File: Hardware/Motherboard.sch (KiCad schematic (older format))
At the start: 22 parts, among them J2 Conn_01x05_Male, J5 Conn_01x04_Male, SW1 SW_Push, SW2 SW_Push, SW3 SW_Push, U1 PIC18F46K22-xPT

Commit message: [Hardware] Added all schematic parts (but not all external parts, like display or female connectors).
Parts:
- added C15: 100n, Capacitor_SMD:C_1206_3216Metric_Pad1.42x1.75mm_HandSolder, symbol Device:C
- added J6: Conn_01x02_Male, Connector_PinHeader_2.54mm:PinHeader_1x02_P2.54mm_Vertical, symbol Connector:Conn_01x02_Male
- J5: footprint (none) -> Connector_PinHeader_2.54mm:PinHeader_1x04_P2.54mm_Vertical
- SW1, SW2, SW3: footprint (none) -> Button_Switch_THT:SW_Tactile_SKHH_Angled
- gave numbers to parts that had none: 3
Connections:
- net +5V: now also C15.1, J6.1 (Pin_1)
- net GND: now also C15.2, J6.2 (Pin_2)
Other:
- note added: "USB power connector.\nUSB D+ and D- are not connected."
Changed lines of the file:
@@
 F 0 "J5" H 5700 6650 50  0000 R CNN
 F 1 "Conn_01x04_Male" H 5700 6750 50  0000 R CNN
-F 2 "" H 5600 6450 50  0001 C CNN
+F 2 "Connector_PinHeader_2.54mm:PinHeader_1x04_P2.54mm_Vertical" H 5600 6450 50  0001 C CNN
 F 3 "~" H 5600 6450 50  0001 C CNN
 	1    5600 6450
@@
 F 0 "SW2" V 2404 1848 50  0000 L CNN
 F 1 "SW_Push" V 2495 1848 50  0000 L CNN
-F 2 "" H 2450 1900 50  0001 C CNN
+F 2 "Button_Switch_THT:SW_Tactile_SKHH_Angled" H 2450 1900 50  0001 C CNN
 F 3 "~" H 2450 1900 50  0001 C CNN
 	1    2450 1700
@@
 F 0 "SW1" V 1804 1848 50  0000 L CNN
 F 1 "SW_Push" V 1895 1848 50  0000 L CNN
-F 2 "" H 1850 1900 50  0001 C CNN
+F 2 "Button_Switch_THT:SW_Tactile_SKHH_Angled" H 1850 1900 50  0001 C CNN
 F 3 "~" H 1850 1900 50  0001 C CNN
 	1    1850 1700
@@
 F 0 "SW3" V 2154 6448 50  0000 L CNN
 F 1 "SW_Push" V 2245 6448 50  0000 L CNN
-F 2 "" H 2200 6500 50  0001 C CNN
+F 2 "Button_Switch_THT:SW_Tactile_SKHH_Angled" H 2200 6500 50  0001 C CNN
 F 3 "~" H 2200 6500 50  0001 C CNN
 	1    2200 6300
@@
 SETTINGS_BUTTON
 $Comp
-L Device:C C?
+L Device:C C12
 U 1 1 5E7D4835
 P 1650 6300
-F 0 "C?" H 1535 6163 50  0000 R CNN
+F 0 "C12" H 1535 6163 50  0000 R CNN
 F 1 "100n" H 1535 6254 50  0000 R CNN
 F 2 "Capacitor_SMD:C_1206_3216Metric_Pad1.42x1.75mm_HandSolder" H 1688 6150 50  0001 C CNN
@@
 $EndComp
 $Comp
-L Device:C C?
+L Device:C C14
 U 1 1 5E7FE585
 P 4950 6700
-F 0 "C?" H 4835 6563 50  0000 R CNN
+F 0 "C14" H 4835 6563 50  0000 R CNN
 F 1 "100n" H 4835 6654 50  0000 R CNN
 F 2 "Capacitor_SMD:C_1206_3216Metric_Pad1.42x1.75mm_HandSolder" H 4988 6550 50  0001 C CNN
@@
 $EndComp
 $Comp
-L Device:C C?
+L Device:C C13
 U 1 1 5E7FF03B
 P 4450 6700
-F 0 "C?" H 4335 6563 50  0000 R CNN
+F 0 "C13" H 4335 6563 50  0000 R CNN
 F 1 "100n" H 4335 6654 50  0000 R CNN
 F 2 "Capacitor_SMD:C_1206_3216Metric_Pad1.42x1.75mm_HandSolder" H 4488 6550 50  0001 C CNN
@@
 	4950 5800 4950 5850
 Connection ~ 4700 5800
+$Comp
+L Connector:Conn_01x02_Male J6
+U 1 1 5E84D5D2
+P 8800 1000
+F 0 "J6" H 8772 974 50  0000 R CNN
+F 1 "Conn_01x02_Male" H 8772 883 50  0000 R CNN
+F 2 "Connector_PinHeader_2.54mm:PinHeader_1x02_P2.54mm_Vertical" H 8800 1000 50  0001 C CNN
+F 3 "~" H 8800 1000 50  0001 C CNN
+	1    8800 1000
+	-1   0    0    -1
+$EndComp
+Text Notes 9600 1100 0    50   ~ 0
+USB power connector.\nUSB D+ and D- are not connected.
+$Comp
+L Device:C C15
+U 1 1 5E853C46
+P 8100 1050
+F 0 "C15" H 8215 1187 50  0000 L CNN
+F 1 "100n" H 8215 1096 50  0000 L CNN
+F 2 "Capacitor_SMD:C_1206_3216Metric_Pad1.42x1.75mm_HandSolder" H 8138 900 50  0001 C CNN
+F 3 "~" H 8100 1050 50  0001 C CNN
+F 4 "25V" H 8215 1005 50  0000 L CNN "Champ4"
+F 5 "X7R" H 8215 914 50  0000 L CNN "Champ5"
+	1    8100 1050
+	1    0    0    -1
+$EndComp
+$Comp
+L power:+5V #PWR09
+U 1 1 5E8541BC
+P 8100 800
+F 0 "#PWR09" H 8100 650 50  0001 C CNN
+F 1 "+5V" H 8115 973 50  0000 C CNN
+F 2 "" H 8100 800 50  0001 C CNN
+F 3 "" H 8100 800 50  0001 C CNN
+	1    8100 800
+	1    0    0    -1
+$EndComp
+$Comp
+L power:GND #PWR010
+U 1 1 5E854558
+P 8100 1300
+F 0 "#PWR010" H 8100 1050 50  0001 C CNN
+F 1 "GND" H 8105 1127 50  0000 C CNN
+F 2 "" H 8100 1300 50  0001 C CNN
+F 3 "" H 8100 1300 50  0001 C CNN
+	1    8100 1300
+	1    0    0    -1
+$EndComp
+Wire Wire Line
+	8100 800  8100 850
+Wire Wire Line
+	8100 850  8550 850
+Wire Wire Line
+	8550 850  8550 1000
+Wire Wire Line
+	8550 1000 8600 1000
+Connection ~ 8100 850
+Wire Wire Line
+	8100 850  8100 900
+Wire Wire Line
+	8600 1100 8550 1100
+Wire Wire Line
+	8550 1100 8550 1250
+Wire Wire Line
+	8550 1250 8100 1250
+Wire Wire Line
+	8100 1250 8100 1200
+Wire Wire Line
+	8100 1250 8100 1300
+Connection ~ 8100 1250
 $EndSCHEMATC

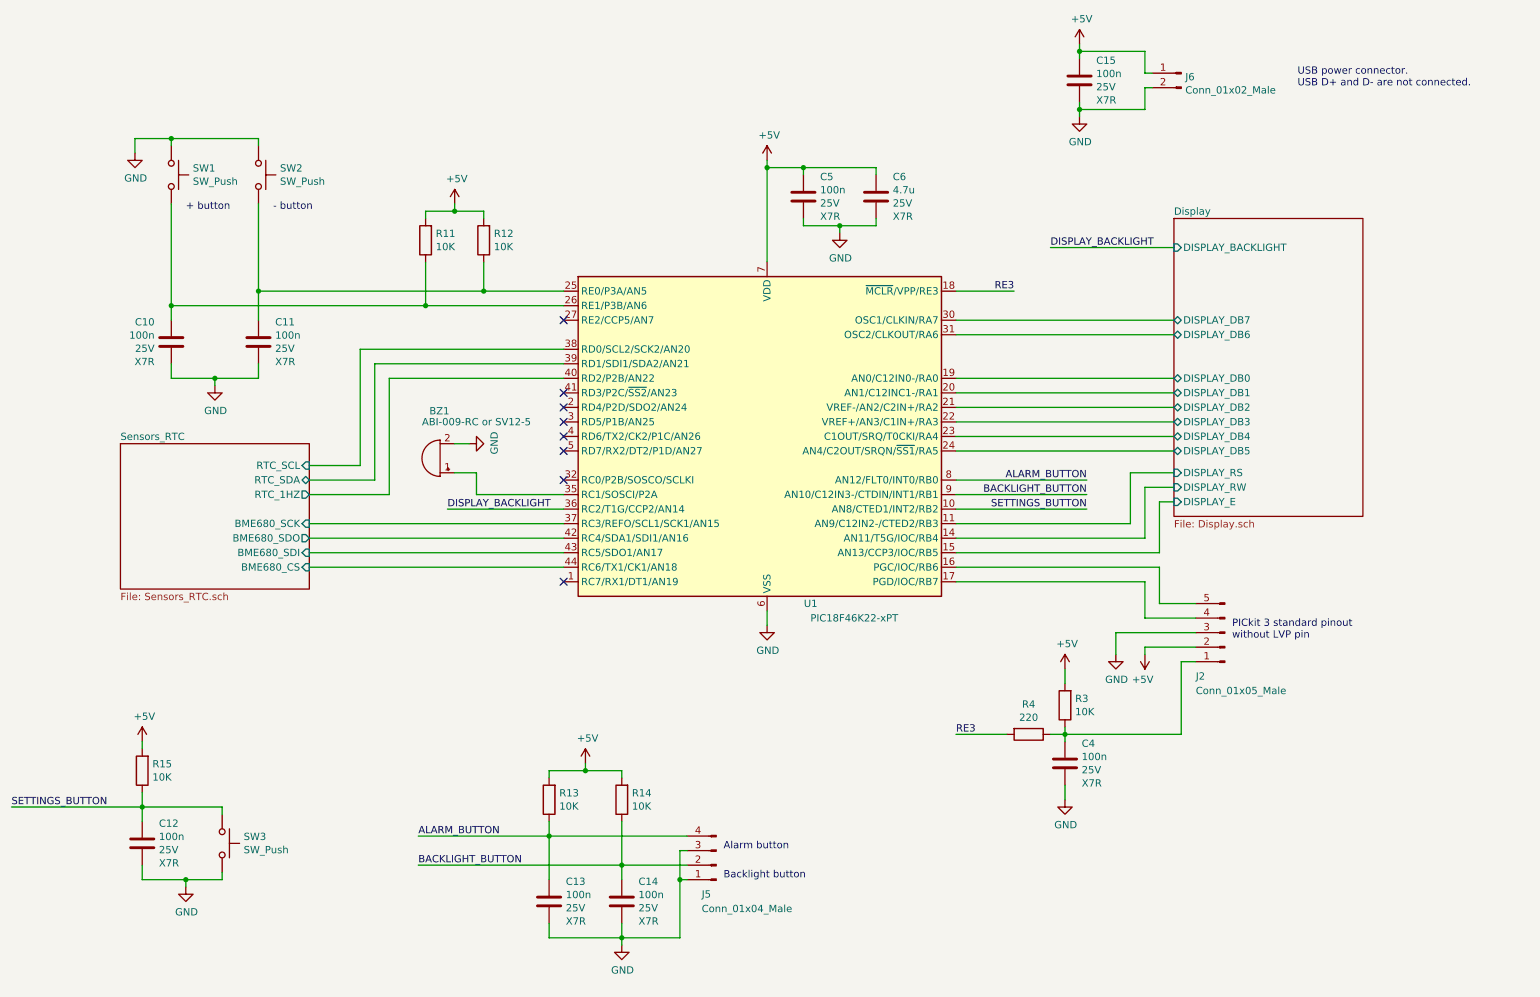
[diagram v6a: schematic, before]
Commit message: [Hardware] Started PCB routing. Components are placed, BME680 board mounting holes are in position, some nets are connected.
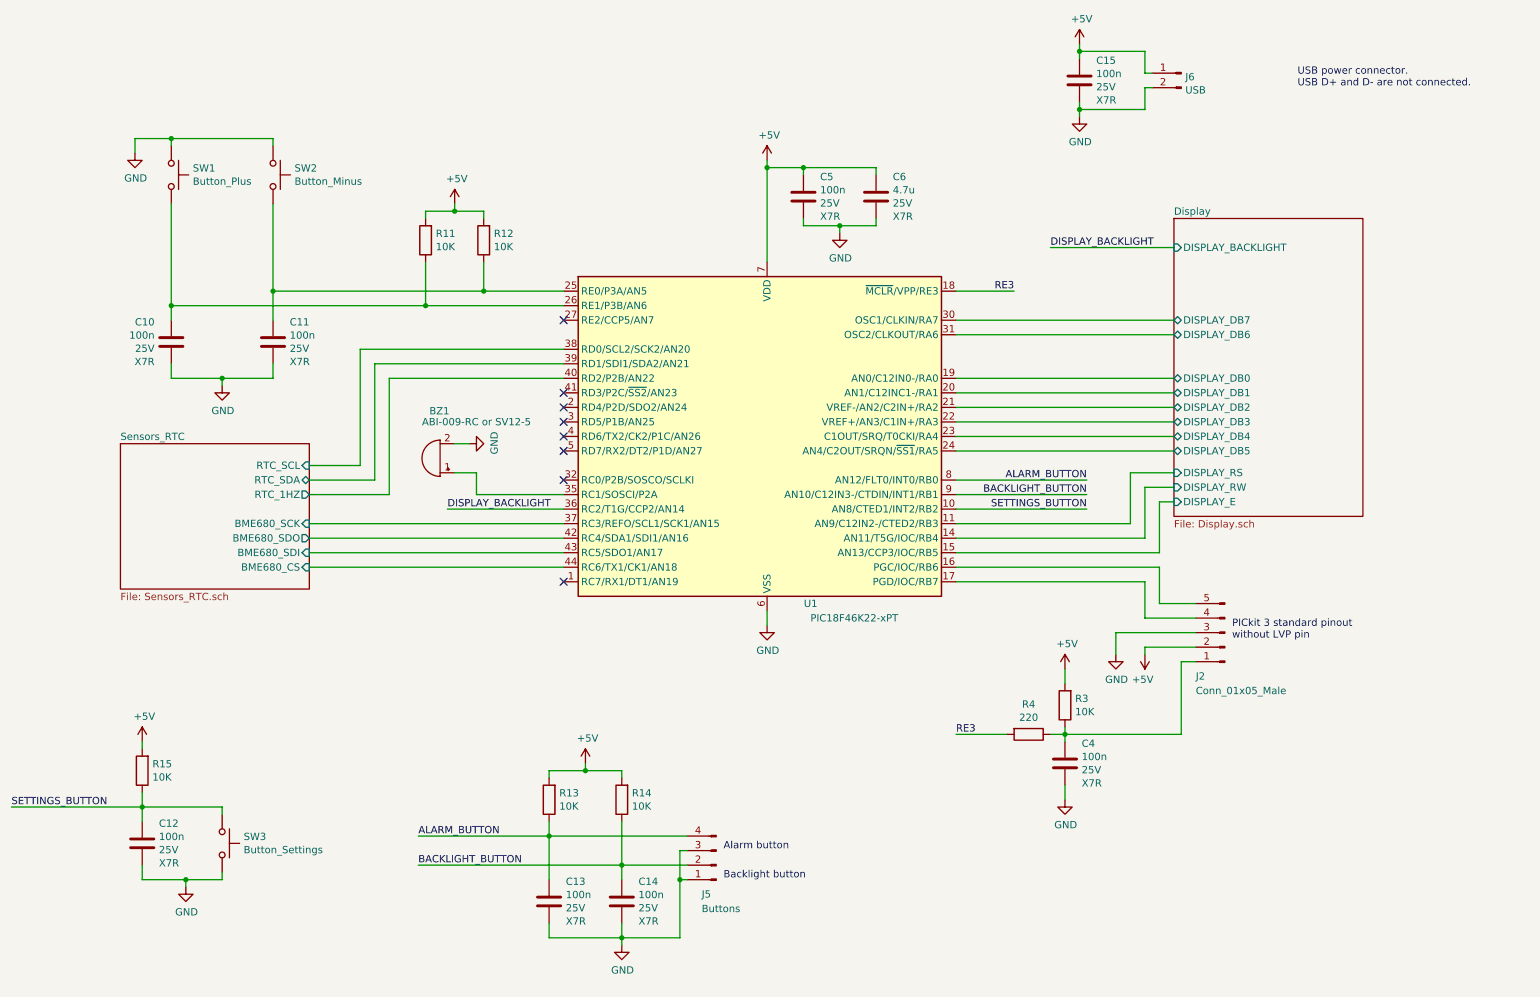
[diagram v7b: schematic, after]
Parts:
- J5: value Conn_01x04_Male -> Buttons
- J6: value Conn_01x02_Male -> USB
- SW1: value SW_Push -> Button_Plus
- SW2: value SW_Push -> Button_Minus
- SW3: value SW_Push -> Button_Settings
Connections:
- net GND: now also SW3.1; no longer SW3.2
- net SETTINGS_BUTTON: now also SW3.2; no longer SW3.1
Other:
- note removed: "+ button"
- note removed: "- button"
- moved on the sheet: C11, SW2
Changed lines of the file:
@@
 P 5600 6450
 F 0 "J5" H 5700 6650 50  0000 R CNN
-F 1 "Conn_01x04_Male" H 5700 6750 50  0000 R CNN
+F 1 "Buttons" H 5700 6750 50  0000 R CNN
 F 2 "Connector_PinHeader_2.54mm:PinHeader_1x04_P2.54mm_Vertical" H 5600 6450 50  0001 C CNN
 F 3 "~" H 5600 6450 50  0001 C CNN
@@
 L Switch:SW_Push SW2
 U 1 1 5E86087F
-P 2450 1700
-F 0 "SW2" V 2404 1848 50  0000 L CNN
-F 1 "SW_Push" V 2495 1848 50  0000 L CNN
-F 2 "Button_Switch_THT:SW_Tactile_SKHH_Angled" H 2450 1900 50  0001 C CNN
-F 3 "~" H 2450 1900 50  0001 C CNN
-	1    2450 1700
+P 2550 1700
+F 0 "SW2" V 2504 1848 50  0000 L CNN
+F 1 "Button_Minus" V 2595 1848 50  0000 L CNN
+F 2 "Button_Switch_THT:SW_Tactile_SKHH_Angled" H 2550 1900 50  0001 C CNN
+F 3 "~" H 2550 1900 50  0001 C CNN
+	1    2550 1700
 	0    1    1    0
 $EndComp
@@
 P 1850 1700
 F 0 "SW1" V 1804 1848 50  0000 L CNN
-F 1 "SW_Push" V 1895 1848 50  0000 L CNN
+F 1 "Button_Plus" V 1895 1848 50  0000 L CNN
 F 2 "Button_Switch_THT:SW_Tactile_SKHH_Angled" H 1850 1900 50  0001 C CNN
 F 3 "~" H 1850 1900 50  0001 C CNN
@@
 U 1 1 5E864A28
 P 2200 6300
-F 0 "SW3" V 2154 6448 50  0000 L CNN
-F 1 "SW_Push" V 2245 6448 50  0000 L CNN
+F 0 "SW3" V 2246 6448 50  0000 L CNN
+F 1 "Button_Settings" V 2155 6448 50  0000 L CNN
 F 2 "Button_Switch_THT:SW_Tactile_SKHH_Angled" H 2200 6500 50  0001 C CNN
 F 3 "~" H 2200 6500 50  0001 C CNN
 	1    2200 6300
-	0    1    1    0
-$EndComp
-Wire Wire Line
-	2450 2500 4000 2500
+	0    1    -1   0
+$EndComp
+Wire Wire Line
+	2550 2500 4000 2500
 Wire Wire Line
 	4550 2600 3600 2600
 Wire Wire Line
-	2450 1500 2450 1450
-Wire Wire Line
-	2450 1450 1850 1450
+	2550 1500 2550 1450
+Wire Wire Line
+	2550 1450 1850 1450
 Wire Wire Line
 	1850 1450 1850 1500
@@
 L Device:C C11
 U 1 1 5E8AB83D
-P 2450 2850
-F 0 "C11" H 2335 2713 50  0000 R CNN
-F 1 "100n" H 2335 2804 50  0000 R CNN
-F 2 "Capacitor_SMD:C_1206_3216Metric_Pad1.42x1.75mm_HandSolder" H 2488 2700 50  0001 C CNN
-F 3 "~" H 2450 2850 50  0001 C CNN
-F 4 "25V" H 2335 2895 50  0000 R CNN "Champ4"
-F 5 "X7R" H 2335 2986 50  0000 R CNN "Champ5"
-	1    2450 2850
+P 2550 2850
+F 0 "C11" H 2435 2713 50  0000 R CNN
+F 1 "100n" H 2435 2804 50  0000 R CNN
+F 2 "Capacitor_SMD:C_1206_3216Metric_Pad1.42x1.75mm_HandSolder" H 2588 2700 50  0001 C CNN
+F 3 "~" H 2550 2850 50  0001 C CNN
+F 4 "25V" H 2435 2895 50  0000 R CNN "Champ4"
+F 5 "X7R" H 2435 2986 50  0000 R CNN "Champ5"
+	1    2550 2850
 	-1   0    0    1
 $EndComp
@@
 L power:GND #PWR03
 U 1 1 5E8AE348
-P 2150 3150
-F 0 "#PWR03" H 2150 2900 50  0001 C CNN
-F 1 "GND" H 2155 2977 50  0000 C CNN
-F 2 "" H 2150 3150 50  0001 C CNN
-F 3 "" H 2150 3150 50  0001 C CNN
-	1    2150 3150
+P 2200 3150
+F 0 "#PWR03" H 2200 2900 50  0001 C CNN
+F 1 "GND" H 2205 2977 50  0000 C CNN
+F 2 "" H 2200 3150 50  0001 C CNN
+F 3 "" H 2200 3150 50  0001 C CNN
+	1    2200 3150
 	1    0    0    -1
 $EndComp
@@
 	1850 3000 1850 3100
 Wire Wire Line
-	2450 3100 2450 3000
+	2550 3100 2550 3000
 $Comp
 L power:GND #PWR01
@@
 	1600 1550 1600 1450
 Wire Wire Line
-	2450 1900 2450 2500
-Wire Wire Line
-	2450 2500 2450 2700
-Connection ~ 2450 2500
+	2550 1900 2550 2500
+Wire Wire Line
+	2550 2500 2550 2700
+Connection ~ 2550 2500
 Wire Wire Line
 	1850 2700 1850 2600
@@
 NoConn ~ 4550 3200
 Wire Wire Line
-	1850 3100 2150 3100
+	1850 3100 2200 3100
 Wire Wire Line
 	1600 1450 1850 1450
 Connection ~ 1850 1450
 Wire Wire Line
-	2150 3150 2150 3100
-Connection ~ 2150 3100
-Wire Wire Line
-	2150 3100 2450 3100
-Text Notes 1950 1950 0    50   ~ 0
-+ button
-Text Notes 2550 1950 0    50   ~ 0
-- button
+	2200 3150 2200 3100
+Connection ~ 2200 3100
+Wire Wire Line
+	2200 3100 2550 3100
 $Comp
 L Device:R R?
@@
 P 8800 1000
 F 0 "J6" H 8772 974 50  0000 R CNN
-F 1 "Conn_01x02_Male" H 8772 883 50  0000 R CNN
+F 1 "USB" H 8772 883 50  0000 R CNN
 F 2 "Connector_PinHeader_2.54mm:PinHeader_1x02_P2.54mm_Vertical" H 8800 1000 50  0001 C CNN
 F 3 "~" H 8800 1000 50  0001 C CNN

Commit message: [Hardware] Moved buttons to another schematic sheet and fully routed PCB.
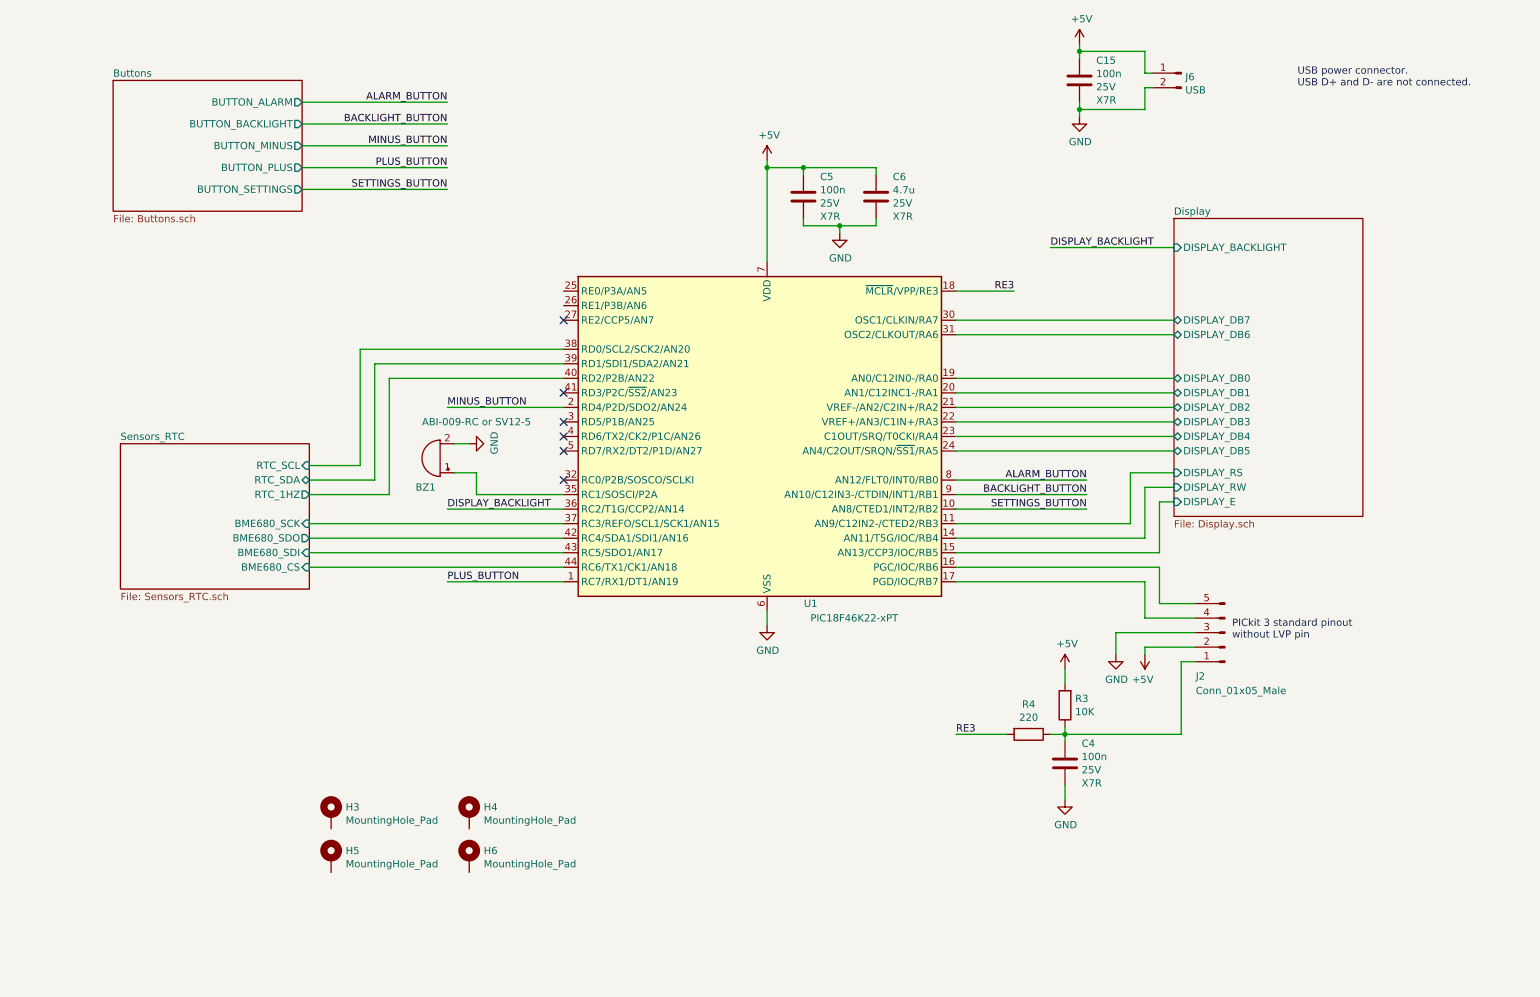
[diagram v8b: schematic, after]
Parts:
- removed C10, C11, C12, C13, C14: 100n, Capacitor_SMD:C_1206_3216Metric_Pad1.42x1.75mm_HandSolder, symbol Device:C
- removed J5: Buttons, Connector_PinHeader_2.54mm:PinHeader_1x04_P2.54mm_Vertical, symbol Connector:Conn_01x04_Male
- removed R11, R12, R13, R14, R15: 10K, Resistor_SMD:R_1206_3216Metric_Pad1.42x1.75mm_HandSolder, symbol Device:R
- removed SW1: Button_Plus, Button_Switch_THT:SW_Tactile_SKHH_Angled, symbol Switch:SW_Push
- removed SW2: Button_Minus, Button_Switch_THT:SW_Tactile_SKHH_Angled, symbol Switch:SW_Push
- removed SW3: Button_Settings, Button_Switch_THT:SW_Tactile_SKHH_Angled, symbol Switch:SW_Push
- added H3, H4, H5, H6: MountingHole_Pad, MountingHole:MountingHole_4.5mm_Pad, symbol Mechanical:MountingHole_Pad
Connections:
- net PLUS_BUTTON: now reaches U1.1 (RC7/RX1/DT1/AN19)
- net MINUS_BUTTON: now reaches U1.2 (RD4/P2D/SDO2/AN24)
- no-connect marks 8 -> 6
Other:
- note removed: "Alarm button"
- note removed: "Backlight button"
